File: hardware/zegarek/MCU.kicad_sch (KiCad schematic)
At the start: 33 parts, among them J3 Conn_01x02, J4 Conn_01x02, J5 Conn_01x04, P1 USB_C_Plug_USB2.0, SW1 SW_Push, U2 STM32F091RCTx, U3 CH340C, Y1 32.768kHz

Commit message: pwr page done
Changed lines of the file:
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@@
-		)
-	)
-	(label "BUZZER"
-		(at 171.45 101.6 180)
-		(effects
-			(font
-				(size 1.27 1.27)
-			)
-			(justify right bottom)
 		)
 	)
@@
 		)
 	)
-	(label "BTNUP"
-		(at 171.45 86.36 180)
-		(effects
-			(font
-				(size 1.27 1.27)
-			)
-			(justify right bottom)
-		)
-	)
 	(label "TMS"
 		(at 171.45 96.52 180)
@@
 	(label "HL_C"
 		(at 162.56 111.76 0)
-		(effects
-			(font
-				(size 1.27 1.27)
-			)
-			(justify left bottom)
-		)
-	)
-	(label "BTNOK"
-		(at 171.45 121.92 180)
-		(effects
-			(font
-				(size 1.27 1.27)
-			)
-			(justify right bottom)
-		)
-	)
-	(label "BTNDN"
-		(at 106.68 101.6 0)
 		(effects
 			(font
@@
 		)
 	)
+	(hierarchical_label "BUZZER"
+		(shape input)
+		(at 171.45 101.6 0)
+		(effects
+			(font
+				(size 1.27 1.27)
+			)
+			(justify left)
+		)
+	)
 	(hierarchical_label "BDC_BUS"
 		(shape output)
@@
 		(effects
 			(font
+				(size 1.27 1.27)
+			)
+			(justify right)
+		)
+	)
+	(hierarchical_label "BTNOK"
+		(shape input)
+		(at 171.45 121.92 0)
+		(effects
+			(font
+				(size 1.27 1.27)
+			)
+			(justify left)
+		)
+	)
+	(hierarchical_label "BTNUP"
+		(shape input)
+		(at 171.45 86.36 0)
+		(effects
+			(font
+				(size 1.27 1.27)
+			)
+			(justify left)
+		)
+	)
+	(hierarchical_label "BTNDN"
+		(shape input)
+		(at 106.68 101.6 180)
+		(effects
+			(font

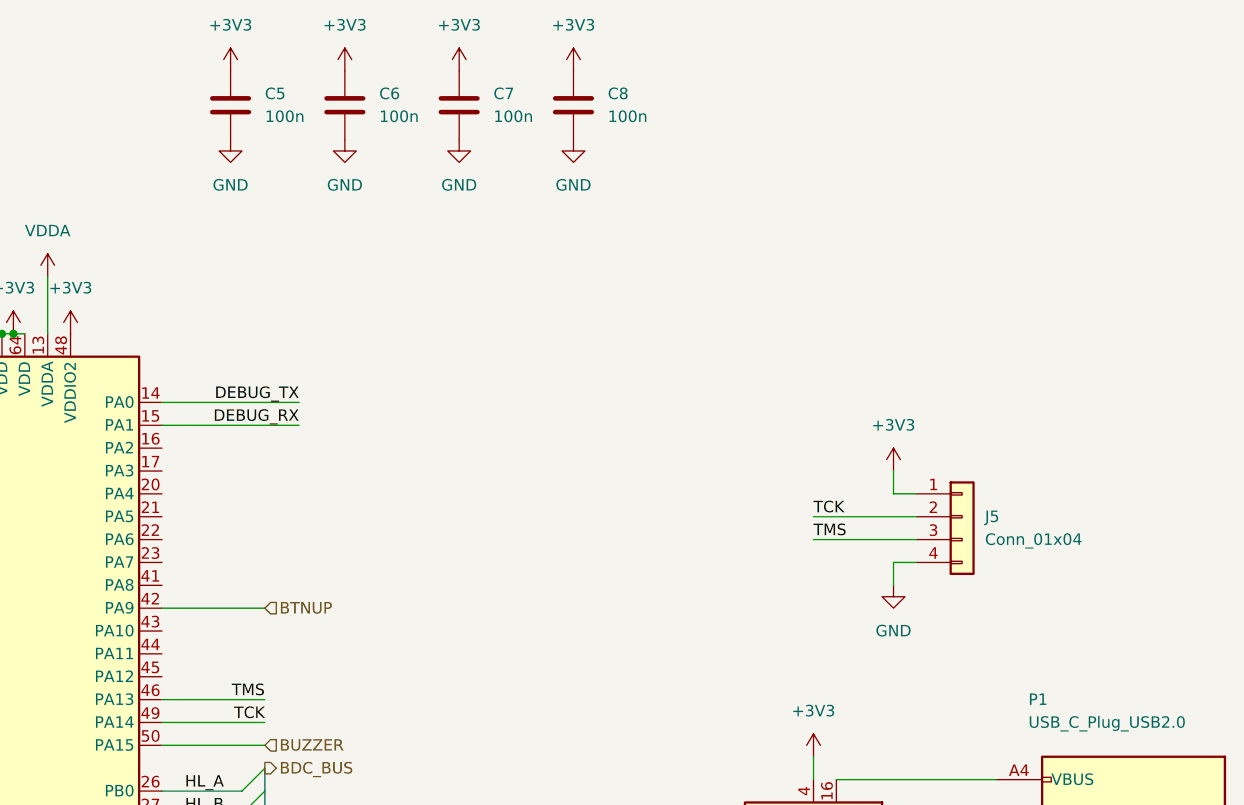
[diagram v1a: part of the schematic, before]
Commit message: added status leds buttons and buzzer, 100V header deleted, footprints assigned
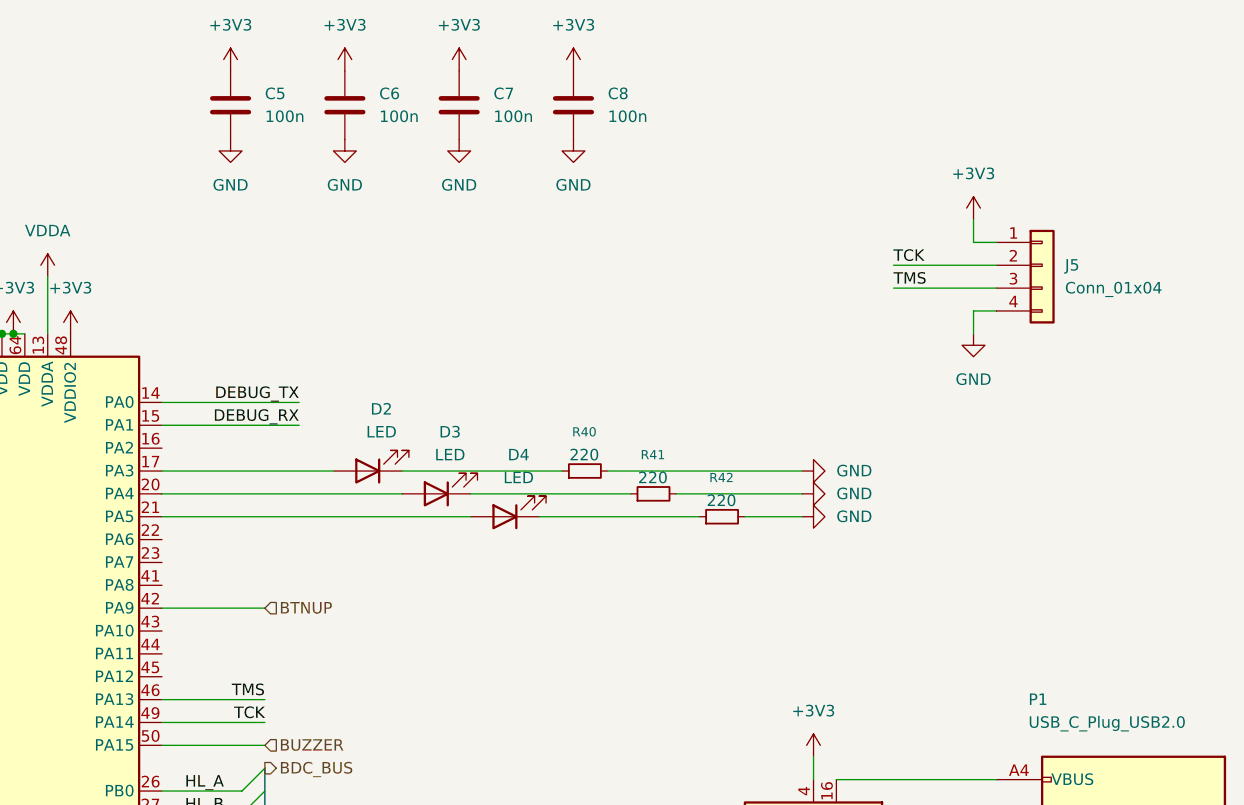
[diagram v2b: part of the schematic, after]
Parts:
- added D2, D3, D4: LED, LED_SMD:LED_0603_1608Metric_Pad1.05x0.95mm_HandSolder, symbol Device:LED
- added R40, R41, R42: 220, Resistor_SMD:R_0201_0603Metric_Pad0.64x0.40mm_HandSolder, symbol Device:R_Small
- BT1: footprint (none) -> Battery:BatteryHolder_MYOUNG_BS-07-A1BJ001_CR2032
- C10, C11, C12, C13, C14, C15, C16, C17, C4, C5, C6, C7, C8, C9: footprint (none) -> Capacitor_SMD:C_1206_3216Metric_Pad1.33x1.80mm_HandSolder
- FB1: footprint (none) -> Inductor_SMD:L_0603_1608Metric_Pad1.05x0.95mm_HandSolder
- J3, J4: footprint (none) -> Connector_PinHeader_2.54mm:PinHeader_1x02_P2.54mm_Vertical
- J5: footprint (none) -> Connector_PinHeader_2.54mm:PinHeader_1x04_P2.54mm_Vertical
- JP1: footprint (none) -> Jumper:SolderJumper-2_P1.3mm_Bridged_RoundedPad1.0x1.5mm
- P1: footprint (none) -> Connector_USB:USB_C_Receptacle_Amphenol_12401948E412A
- R10, R11, R12, R6, R7, R8, R9: footprint (none) -> Resistor_SMD:R_0201_0603Metric_Pad0.64x0.40mm_HandSolder
- SW1: footprint (none) -> Button_Switch_SMD:SW_Push_1P1T_NO_CK_KMR2
- TP1: footprint (none) -> TestPoint:TestPoint_Pad_1.0x1.0mm
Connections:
- net GND: now also R40.2, R41.2, R42.2
- net at U2.17 (PA3): now also D2.2 (A)
- net at U2.20 (PA4): now also D3.2 (A)
- net at U2.21 (PA5): now also D4.2 (A)
- new net: D2.1 (K), R40.1
- new net: D3.1 (K), R41.1
- new net: D4.1 (K), R42.1
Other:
- moved on the sheet: J5

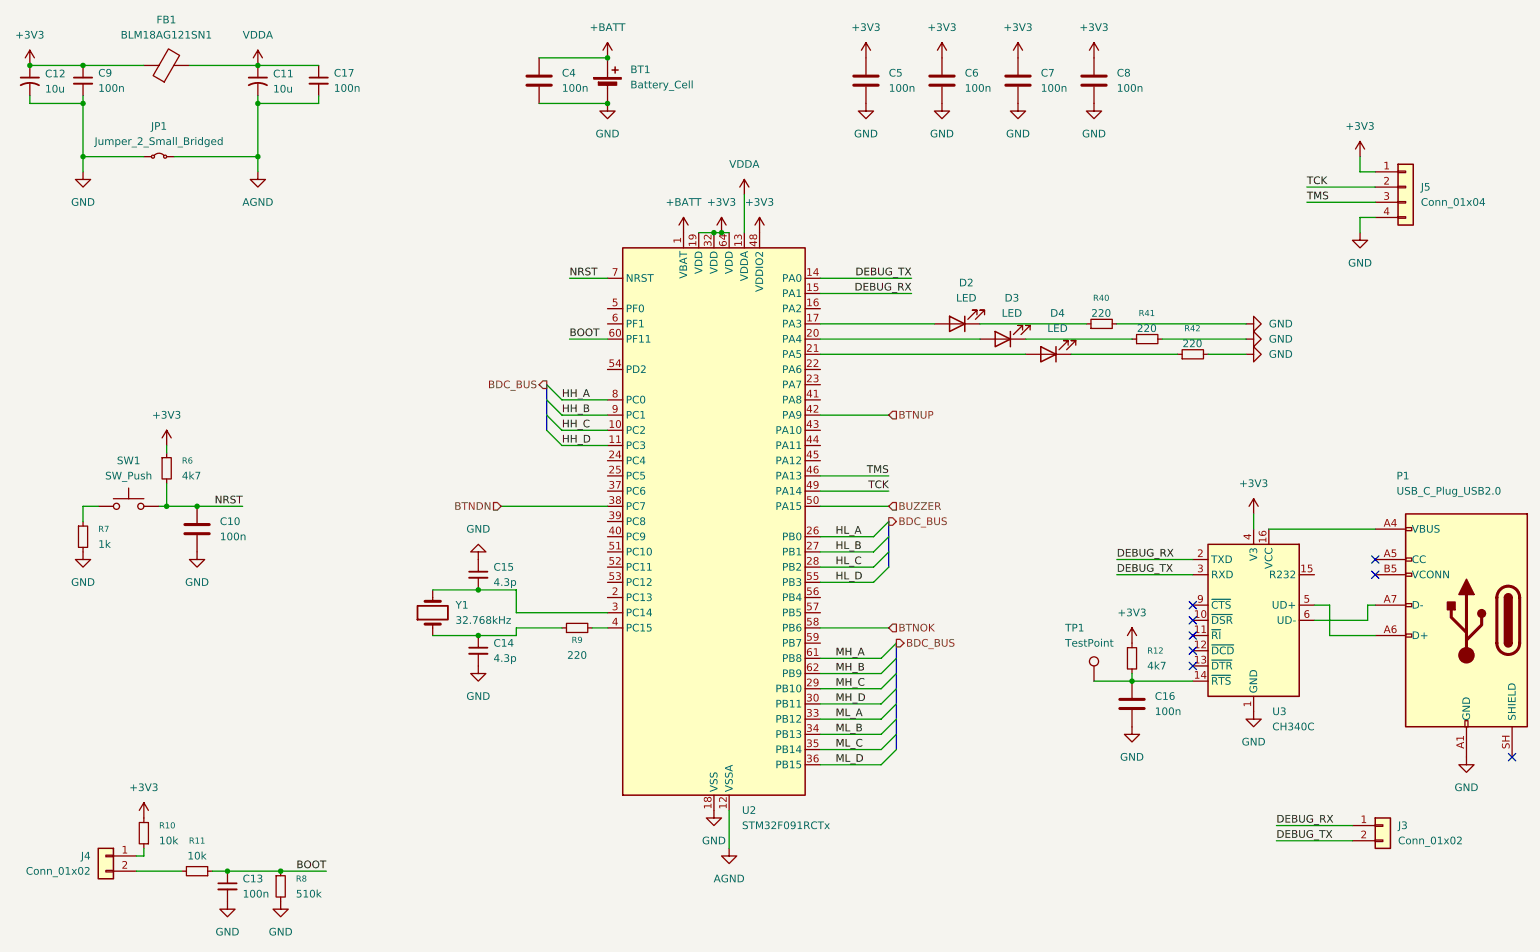
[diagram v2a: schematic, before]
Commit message: done placing footprins on pcb, started tracing pcb
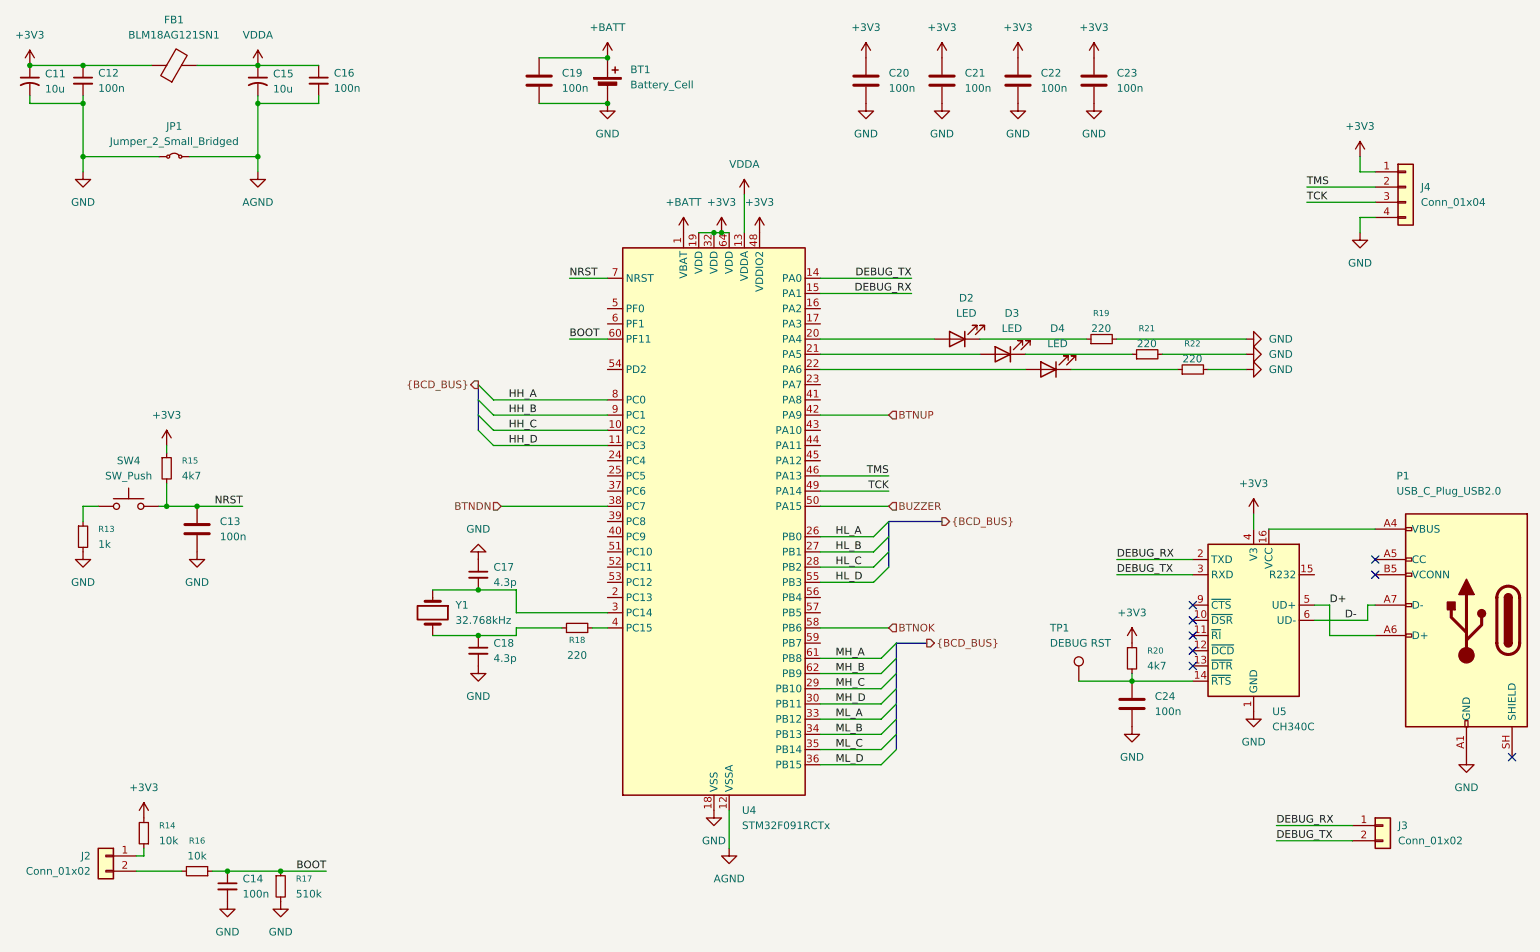
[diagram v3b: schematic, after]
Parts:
- R13: renamed from R7; footprint Resistor_SMD:R_0201_0603Metric_Pad0.64x0.40mm_HandSolder -> Resistor_SMD:R_0603_1608Metric_Pad0.98x0.95mm_HandSolder
- R14: renamed from R10; footprint Resistor_SMD:R_0201_0603Metric_Pad0.64x0.40mm_HandSolder -> Resistor_SMD:R_0603_1608Metric_Pad0.98x0.95mm_HandSolder
- R15: renamed from R6; footprint Resistor_SMD:R_0201_0603Metric_Pad0.64x0.40mm_HandSolder -> Resistor_SMD:R_0603_1608Metric_Pad0.98x0.95mm_HandSolder
- R16: renamed from R11; footprint Resistor_SMD:R_0201_0603Metric_Pad0.64x0.40mm_HandSolder -> Resistor_SMD:R_0603_1608Metric_Pad0.98x0.95mm_HandSolder
- R17: renamed from R8; footprint Resistor_SMD:R_0201_0603Metric_Pad0.64x0.40mm_HandSolder -> Resistor_SMD:R_0603_1608Metric_Pad0.98x0.95mm_HandSolder
- R18: renamed from R9; footprint Resistor_SMD:R_0201_0603Metric_Pad0.64x0.40mm_HandSolder -> Resistor_SMD:R_0603_1608Metric_Pad0.98x0.95mm_HandSolder
- R19: renamed from R40; footprint Resistor_SMD:R_0201_0603Metric_Pad0.64x0.40mm_HandSolder -> Resistor_SMD:R_0603_1608Metric_Pad0.98x0.95mm_HandSolder
- R20: renamed from R12; footprint Resistor_SMD:R_0201_0603Metric_Pad0.64x0.40mm_HandSolder -> Resistor_SMD:R_0603_1608Metric_Pad0.98x0.95mm_HandSolder
- R21: renamed from R41; footprint Resistor_SMD:R_0201_0603Metric_Pad0.64x0.40mm_HandSolder -> Resistor_SMD:R_0603_1608Metric_Pad0.98x0.95mm_HandSolder
- R22: renamed from R42; footprint Resistor_SMD:R_0201_0603Metric_Pad0.64x0.40mm_HandSolder -> Resistor_SMD:R_0603_1608Metric_Pad0.98x0.95mm_HandSolder
- TP1: value TestPoint -> DEBUG RST; footprint TestPoint:TestPoint_Pad_1.0x1.0mm -> TestPoint:TestPoint_Loop_D2.60mm_Drill0.9mm_Beaded
- Y1: footprint Crystal:Crystal_AT310_D3.0mm_L10.0mm_Horizontal_1EP_style1 -> Crystal:Crystal_AT310_D3.0mm_L10.0mm_Horizontal
- renumbered C12 to C11, C9 to C12, C10 to C13, C13 to C14, C11 to C15, C17 to C16, C15 to C17, C14 to C18, C4 to C19, C5 to C20, C6 to C21, C7 to C22, C8 to C23, C16 to C24, J4 to J2, J5 to J4, SW1 to SW4, U2 to U4, U3 to U5
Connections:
- net TCK: now also J4.3 (Pin_3); no longer J4.2 (Pin_2)
- net TMS: now also J4.2 (Pin_2); no longer J4.3 (Pin_3)
- net D+: now reaches P1.A6 (D+), U5.5 (UD+)
- net D-: now reaches P1.A7 (D-), U5.6 (UD-)
- net at C18.1, R18.1: now also Y1.2; no longer Y1.1
- net at D3.2 (A): now also U4.21 (PA5); no longer U4.20 (PA4)
- net at D4.2 (A): now also U4.22 (PA6); no longer U4.21 (PA5)
- net at C17.2, U4.3 (PC14): now also Y1.1; no longer Y1.2
- net at D2.2 (A): now also U4.20 (PA4); no longer U4.17 (PA3)
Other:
- moved on the sheet: D2, D3, D4, FB1, JP1, R19, R21, R22, TP1, Y1

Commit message: jlc generated bom and grb+drill
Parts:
- BT1: LCSC (none) -> C964750
- C11, C15: LCSC (none) -> C49326738
- C12, C14, C16, C19, C20, C21, C22, C23, C24: LCSC (none) -> C152824
- C13: footprint Capacitor_SMD:C_1206_3216Metric_Pad1.33x1.80mm_HandSolder -> Capacitor_SMD:C_0603_1608Metric_Pad1.08x0.95mm_HandSolder; LCSC (none) -> C1590
- C17, C18: footprint Capacitor_SMD:C_1206_3216Metric_Pad1.33x1.80mm_HandSolder -> Capacitor_SMD:C_0603_1608Metric_Pad1.08x0.95mm_HandSolder; LCSC (none) -> C424850
- D2: LCSC (none) -> C89811
- D3: LCSC (none) -> C2286
- D4: LCSC (none) -> C2288
- FB1: LCSC (none) -> C76892
- J2, J3: LCSC (none) -> C86471
- J4: LCSC (none) -> C124378
- P1: LCSC (none) -> C53185062
- R13: LCSC (none) -> C2074140
- R14, R16: LCSC (none) -> C15401
- R15, R20: LCSC (none) -> C3152147
- R17: LCSC (none) -> C23192
- R18, R19, R21, R22: LCSC (none) -> C54920883
- U4: LCSC (none) -> C89056
- U5: LCSC (none) -> C84681
- Y1: LCSC (none) -> C2236
